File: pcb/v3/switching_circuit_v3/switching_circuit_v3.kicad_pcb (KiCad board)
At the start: 2 copper layers, 128 parts, among them J2a1 Cell+, J2b1 Cell-, J3 OLED, J4 microSD, Q1 AO3400A, Q2 AO3400A, Q3 AO3400A, Q4 AO3400A, U1 UCC5304DWVR, U2 UCC5304DWVR, U3 UCC5304DWVR, U4 UCC5304DWVR

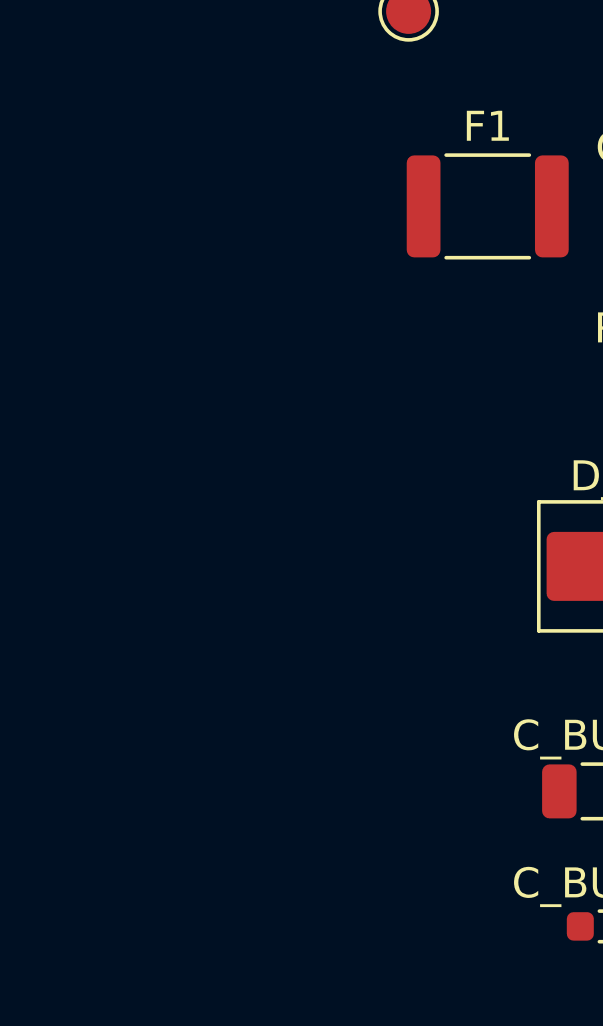
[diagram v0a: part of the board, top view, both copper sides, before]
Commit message: V3: add placement guide, update KiCad layout and schematic
Add pcb/v3/PLACEMENT_GUIDE.md with checkboxed component placement map
organized by functional block (protection, power stage, gate drivers,
analog front-end, MCU, peripherals) for KiCad layout reference.

Co-Authored-By: Claude Opus 4.6 (1M context) <noreply@anthropic.com>
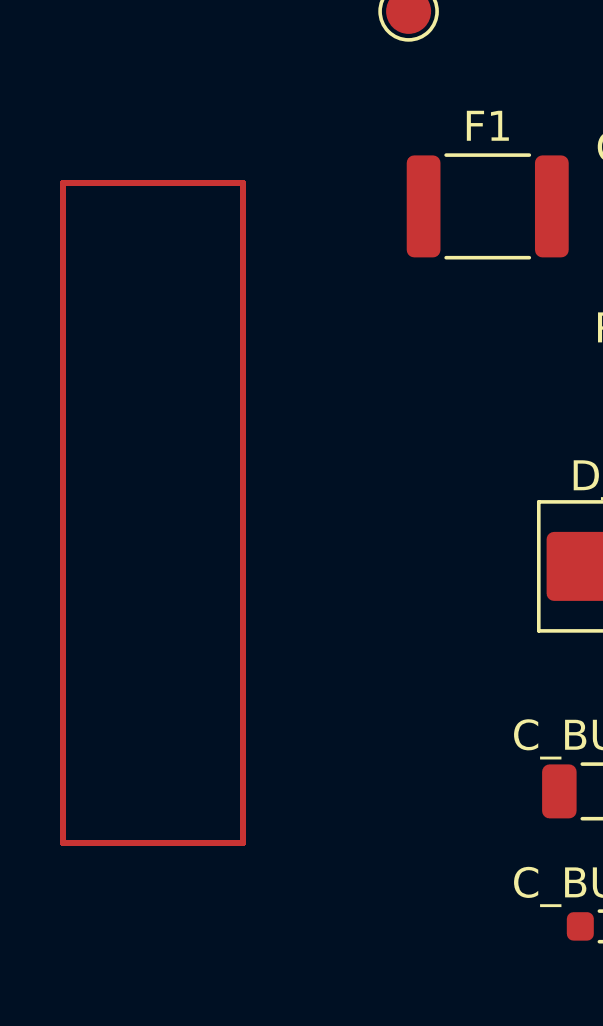
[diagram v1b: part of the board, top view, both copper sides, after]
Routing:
- added copper zone on F.Cu, net CYCLER_IN+
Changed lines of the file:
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@@
+		)
+	)
+	(gr_rect
+		(start 16.5 106)
+		(end 22.5 128)
+		(stroke
+			(width 0.2)
+			(type default)
+		)
+		(fill no)
+		(layer "F.Cu")
+	)
+	(zone
+		(net "CYCLER_IN+")
+		(layer "F.Cu")
+		(name "In_pad_+")
+		(hatch edge 0.5)
+		(connect_pads
+			(clearance 0.5)
+		)
+		(min_thickness 0.25)
+		(fill
+			(thermal_gap 0.5)
+			(thermal_bridge_width 0.5)
+			(island_removal_mode 0)
+		)
+		(polygon
+			(pts
+				(xy 16.5 106) (xy 22.5 106) (xy 22.5 128) (xy 16.5 128)
+			)
 		)
 	)
